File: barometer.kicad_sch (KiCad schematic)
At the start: 2 parts, among them U5 MS5637-02BA03

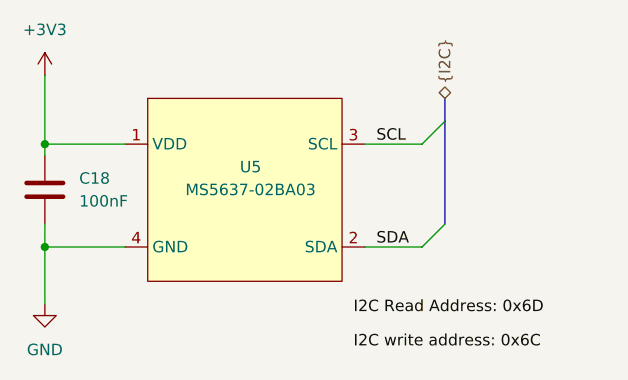
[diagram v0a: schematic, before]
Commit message: Geographical reannotated
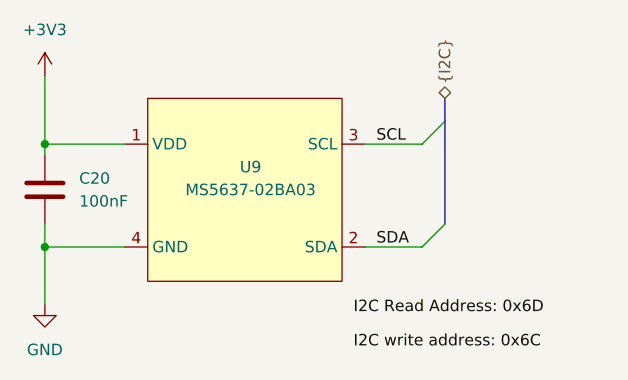
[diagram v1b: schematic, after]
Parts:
- renumbered C18 to C20, U5 to U9
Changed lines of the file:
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@@
   (symbol (lib_id "Sensor:MS5637-02BA03") (at 127 69.85 0) (unit 1)
     (in_bom yes) (on_board yes)
-    (property "Reference" "U5" (id 0) (at 129.54 78.74 0))
+    (property "Reference" "U9" (id 0) (at 129.54 78.74 0))
     (property "Value" "MS5637-02BA03" (id 1) (at 129.54 81.28 0))
     (property "Footprint" "YAR_Sensors:MS5637_1" (id 2) (at 127 69.85 0)
@@
   (symbol (lib_id "Device:C") (at 106.68 81.28 0) (unit 1)
     (in_bom yes) (on_board yes) (fields_autoplaced)
-    (property "Reference" "C18" (id 0) (at 110.49 80.0099 0)
+    (property "Reference" "C20" (id 0) (at 110.49 80.0099 0)
       (effects (font (size 1.27 1.27)) (justify left))
     )

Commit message: Final refinements before issue to JLC
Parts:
- renumbered C20 to C18, U9 to U5
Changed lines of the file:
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@@
   (symbol (lib_id "power:+3V3") (at 106.68 68.58 0) (unit 1)
     (in_bom yes) (on_board yes) (fields_autoplaced)
-    (property "Reference" "#PWR036" (id 0) (at 106.68 72.39 0)
+    (property "Reference" "#PWR038" (id 0) (at 106.68 72.39 0)
       (effects (font (size 1.27 1.27)) hide)
     )
@@
   (symbol (lib_id "Sensor:MS5637-02BA03") (at 127 69.85 0) (unit 1)
     (in_bom yes) (on_board yes)
-    (property "Reference" "U9" (id 0) (at 129.54 78.74 0))
+    (property "Reference" "U5" (id 0) (at 129.54 78.74 0))
     (property "Value" "MS5637-02BA03" (id 1) (at 129.54 81.28 0))
     (property "Footprint" "YAR_Sensors:MS5637_1" (id 2) (at 127 69.85 0)
@@
   (symbol (lib_id "Device:C") (at 106.68 81.28 0) (unit 1)
     (in_bom yes) (on_board yes) (fields_autoplaced)
-    (property "Reference" "C20" (id 0) (at 110.49 80.0099 0)
+    (property "Reference" "C18" (id 0) (at 110.49 80.0099 0)
       (effects (font (size 1.27 1.27)) (justify left))
     )
@@
   (symbol (lib_id "power:GND") (at 106.68 93.98 0) (unit 1)
     (in_bom yes) (on_board yes) (fields_autoplaced)
-    (property "Reference" "#PWR037" (id 0) (at 106.68 100.33 0)
+    (property "Reference" "#PWR039" (id 0) (at 106.68 100.33 0)
       (effects (font (size 1.27 1.27)) hide)
     )
